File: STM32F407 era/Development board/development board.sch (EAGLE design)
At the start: 95 parts, among them IC1 74HC595N, IC2 74HC595N, IC3 317T, IC4 317T, U1 MAX13052ESA+, X1 K375M, X2 HD44780LCD-1602, X3 SDBMF, X4 057-006-1, X5 PN61729-S, X8 057-006-1, X9 057-006-1

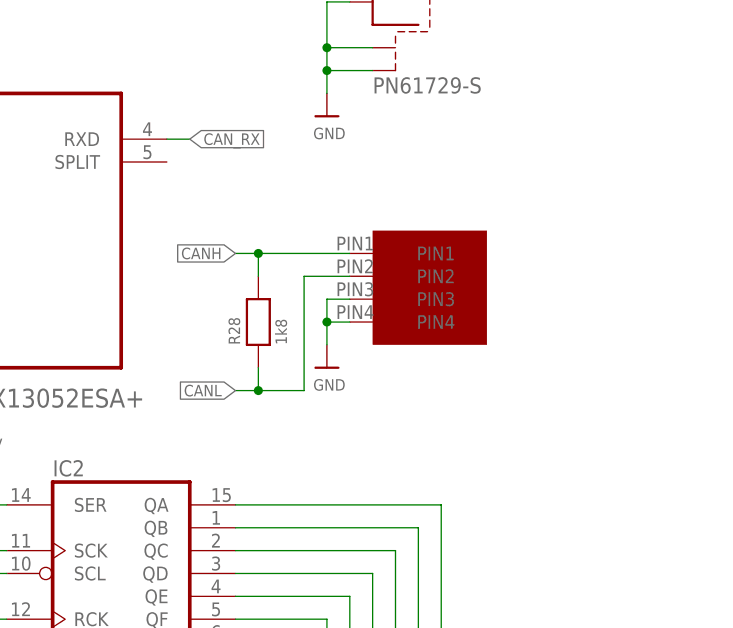
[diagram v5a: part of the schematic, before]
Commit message: change impendance layout for CAN transciever
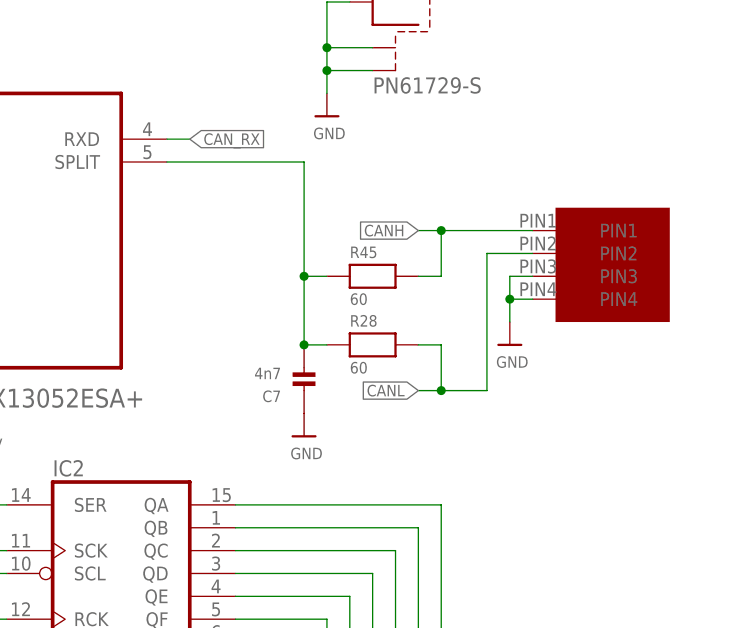
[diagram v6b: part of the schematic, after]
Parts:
- added C7: 4n7, microbuilder:CAP_CERAMIC_0603
- added R45: 60, microbuilder:RESISTOR_0603
- R28: value 1k8 -> 60
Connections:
- new net N$72: C7.P$2, R28.1, R45.1, U1.SPLIT
- net CANH: now also R45.2; no longer R28.2
- net CANL: now also R28.2; no longer R28.1
- net GND: now also C7.P$1
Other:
- moved on the sheet: R28
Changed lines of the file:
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@@
 <part name="U$59" library="microbuilder" deviceset="GND" device=""/>
 <part name="U$60" library="microbuilder" deviceset="GND" device=""/>
-<part name="R28" library="microbuilder" deviceset="RESISTOR" device="_0603" value="1k8"/>
 <part name="ISP1" library="adafruit" deviceset="AVRISP" device="-BOX"/>
 <part name="U$61" library="microbuilder" deviceset="GND" device=""/>
@@
 <part name="R43" library="microbuilder" deviceset="RESISTOR" device="_0603" value="120"/>
 <part name="R44" library="microbuilder" deviceset="RESISTOR" device="_0603" value="120"/>
+<part name="R28" library="microbuilder" deviceset="RESISTOR" device="_0603" value="60"/>
+<part name="R45" library="microbuilder" deviceset="RESISTOR" device="_0603" value="60"/>
+<part name="C7" library="microbuilder" deviceset="CAP_CERAMIC" device="_0603" value="4n7"/>
+<part name="U$64" library="microbuilder" deviceset="GND" device=""/>
 </parts>
 <sheets>
@@
 <instance part="U$56" gate="G$1" x="22.86" y="-43.18"/>
 <instance part="U1" gate="A" x="220.98" y="-50.8"/>
-<instance part="U$57" gate="G$1" x="266.7" y="-60.96"/>
+<instance part="U$57" gate="G$1" x="287.02" y="-58.42"/>
 <instance part="U$58" gate="G$1" x="200.66" y="-38.1"/>
 <instance part="U$59" gate="G$1" x="200.66" y="-68.58"/>
-<instance part="U$60" gate="G$1" x="256.54" y="-68.58"/>
-<instance part="R28" gate="G$1" x="248.92" y="-63.5" rot="R90"/>
+<instance part="U$60" gate="G$1" x="276.86" y="-66.04"/>
 <instance part="ISP1" gate="G$1" x="269.24" y="2.54"/>
 <instance part="U$61" gate="G$1" x="287.02" y="-5.08"/>
@@
 <instance part="R43" gate="G$1" x="266.7" y="-106.68" rot="R270"/>
 <instance part="R44" gate="G$1" x="269.24" y="-106.68" rot="R270"/>
+<instance part="R28" gate="G$1" x="261.62" y="-66.04"/>
+<instance part="R45" gate="G$1" x="261.62" y="-58.42"/>
+<instance part="C7" gate="G$1" x="254" y="-68.58" rot="R180"/>
+<instance part="U$64" gate="G$1" x="254" y="-76.2"/>
 </instances>
 <busses>
@@
 <pinref part="U$57" gate="G$1" pin="PIN4"/>
 <pinref part="U$60" gate="G$1" pin="GND"/>
-<wire x1="259.08" y1="-63.5" x2="256.54" y2="-63.5" width="0.1524" layer="91"/>
-<wire x1="256.54" y1="-63.5" x2="256.54" y2="-66.04" width="0.1524" layer="91"/>
+<wire x1="279.4" y1="-60.96" x2="276.86" y2="-60.96" width="0.1524" layer="91"/>
+<wire x1="276.86" y1="-60.96" x2="276.86" y2="-63.5" width="0.1524" layer="91"/>
 <pinref part="U$57" gate="G$1" pin="PIN3"/>
-<wire x1="259.08" y1="-60.96" x2="256.54" y2="-60.96" width="0.1524" layer="91"/>
-<wire x1="256.54" y1="-60.96" x2="256.54" y2="-63.5" width="0.1524" layer="91"/>
-<junction x="256.54" y="-63.5"/>
+<wire x1="279.4" y1="-58.42" x2="276.86" y2="-58.42" width="0.1524" layer="91"/>
+<wire x1="276.86" y1="-58.42" x2="276.86" y2="-60.96" width="0.1524" layer="91"/>
+<junction x="276.86" y="-60.96"/>
 </segment>
 <segment>
@@
 <wire x1="137.16" y1="-25.4" x2="142.24" y2="-25.4" width="0.1524" layer="91"/>
 <junction x="142.24" y="-25.4"/>
+</segment>
+<segment>
+<pinref part="C7" gate="G$1" pin="P$1"/>
+<pinref part="U$64" gate="G$1" pin="GND"/>
 </segment>
 </net>
@@
 <segment>
 <pinref part="U$57" gate="G$1" pin="PIN2"/>
-<wire x1="246.38" y1="-71.12" x2="248.92" y2="-71.12" width="0.1524" layer="91"/>
-<wire x1="248.92" y1="-71.12" x2="254" y2="-71.12" width="0.1524" layer="91"/>
-<wire x1="254" y1="-71.12" x2="254" y2="-58.42" width="0.1524" layer="91"/>
-<wire x1="254" y1="-58.42" x2="259.08" y2="-58.42" width="0.1524" layer="91"/>
-<label x="246.38" y="-71.12" size="1.27" layer="95" rot="R180" xref="yes"/>
-<pinref part="R28" gate="G$1" pin="1"/>
-<wire x1="248.92" y1="-68.58" x2="248.92" y2="-71.12" width="0.1524" layer="91"/>
-<junction x="248.92" y="-71.12"/>
+<wire x1="266.7" y1="-71.12" x2="269.24" y2="-71.12" width="0.1524" layer="91"/>
+<wire x1="269.24" y1="-71.12" x2="274.32" y2="-71.12" width="0.1524" layer="91"/>
+<wire x1="274.32" y1="-71.12" x2="274.32" y2="-55.88" width="0.1524" layer="91"/>
+<wire x1="274.32" y1="-55.88" x2="279.4" y2="-55.88" width="0.1524" layer="91"/>
+<label x="266.7" y="-71.12" size="1.27" layer="95" rot="R180" xref="yes"/>
+<junction x="269.24" y="-71.12"/>
+<pinref part="R28" gate="G$1" pin="2"/>
+<wire x1="266.7" y1="-66.04" x2="269.24" y2="-66.04" width="0.1524" layer="91"/>
+<wire x1="269.24" y1="-66.04" x2="269.24" y2="-71.12" width="0.1524" layer="91"/>
 </segment>
 </net>
@@
 <segment>
 <pinref part="U$57" gate="G$1" pin="PIN1"/>
-<wire x1="246.38" y1="-55.88" x2="248.92" y2="-55.88" width="0.1524" layer="91"/>
-<label x="246.38" y="-55.88" size="1.27" layer="95" rot="R180" xref="yes"/>
-<pinref part="R28" gate="G$1" pin="2"/>
-<wire x1="248.92" y1="-55.88" x2="259.08" y2="-55.88" width="0.1524" layer="91"/>
-<wire x1="248.92" y1="-55.88" x2="248.92" y2="-58.42" width="0.1524" layer="91"/>
-<junction x="248.92" y="-55.88"/>
+<wire x1="266.7" y1="-53.34" x2="269.24" y2="-53.34" width="0.1524" layer="91"/>
+<label x="266.7" y="-53.34" size="1.27" layer="95" rot="R180" xref="yes"/>
+<wire x1="269.24" y1="-53.34" x2="279.4" y2="-53.34" width="0.1524" layer="91"/>
+<junction x="269.24" y="-53.34"/>
+<pinref part="R45" gate="G$1" pin="2"/>
+<wire x1="266.7" y1="-58.42" x2="269.24" y2="-58.42" width="0.1524" layer="91"/>
+<wire x1="269.24" y1="-58.42" x2="269.24" y2="-53.34" width="0.1524" layer="91"/>
 </segment>
 </net>
@@
 </segment>
 </net>
+<net name="N$72" class="0">
+<segment>
+<pinref part="R28" gate="G$1" pin="1"/>
+<wire x1="256.54" y1="-66.04" x2="254" y2="-66.04" width="0.1524" layer="91"/>
+<wire x1="254" y1="-66.04" x2="254" y2="-58.42" width="0.1524" layer="91"/>
+<pinref part="R45" gate="G$1" pin="1"/>
+<wire x1="254" y1="-58.42" x2="256.54" y2="-58.42" width="0.1524" layer="91"/>
+<pinref part="U1" gate="A" pin="SPLIT"/>
+<wire x1="238.76" y1="-45.72" x2="254" y2="-45.72" width="0.1524" layer="91"/>
+<wire x1="254" y1="-45.72" x2="254" y2="-58.42" width="0.1524" layer="91"/>
+<junction x="254" y="-58.42"/>
+<pinref part="C7" gate="G$1" pin="P$2"/>
+<junction x="254" y="-66.04"/>
+</segment>
+</net>

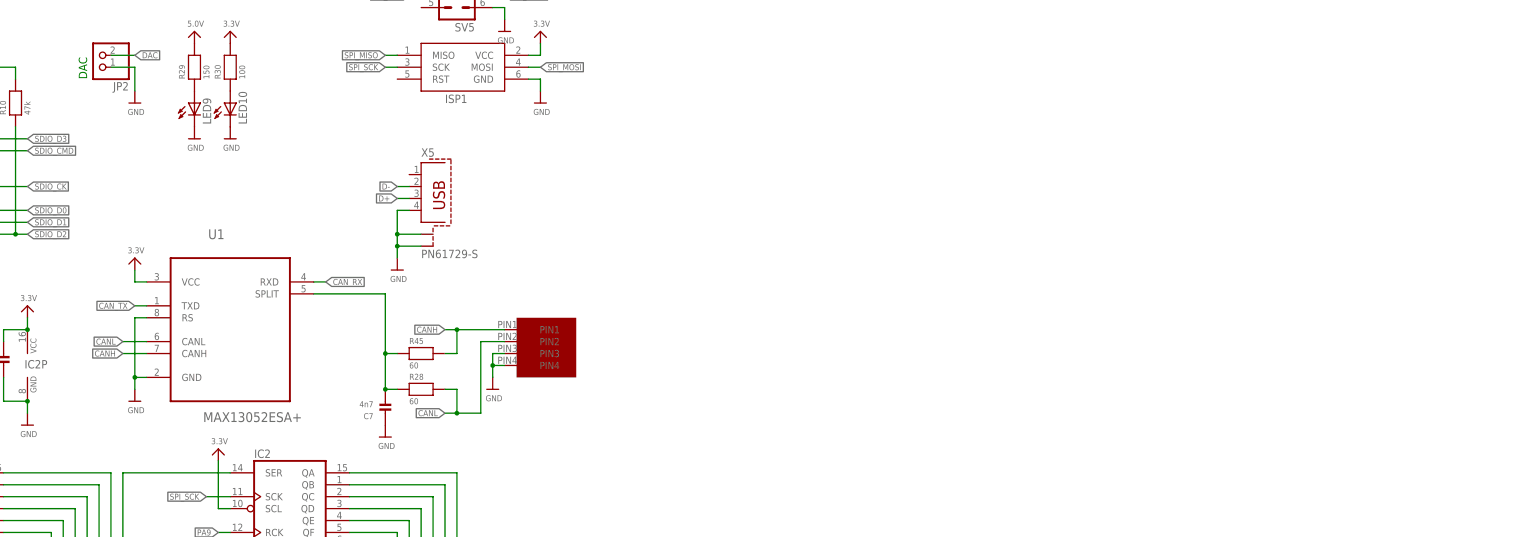
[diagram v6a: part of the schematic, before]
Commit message: succeded in removing one of 2 connectors
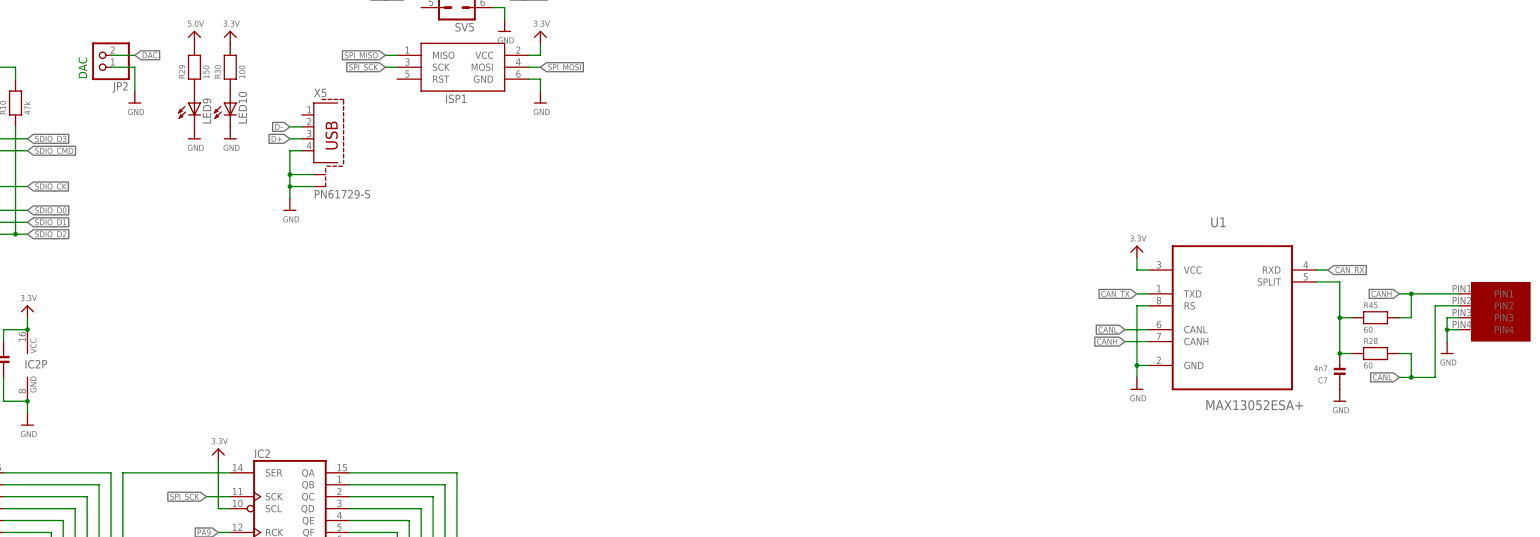
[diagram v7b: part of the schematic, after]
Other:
- moved on the sheet: C7, R28, R45, U1, X5
